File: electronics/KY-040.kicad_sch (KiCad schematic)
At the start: 8 parts, among them SW2 PEC12R-4220F-S0024

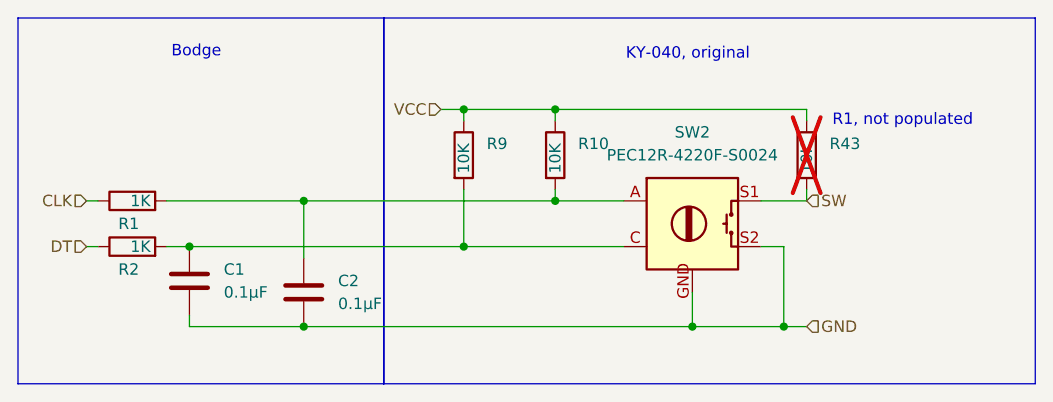
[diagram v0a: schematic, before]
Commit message: docs(electronics): label KY-040 resistors
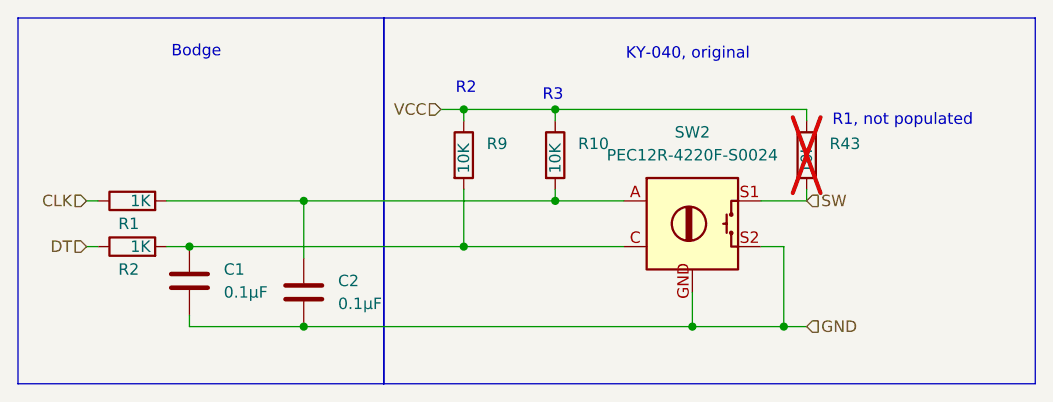
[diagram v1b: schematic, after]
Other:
- note added: "R2"
- note added: "R3"
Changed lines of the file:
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@@
+		)
+	)
+	(text "R2"
+		(exclude_from_sim no)
+		(at 70.104 89.154 0)
+		(effects
+			(font
+				(size 1.27 1.27)
+			)
+		)
+	)
+	(text "R3"
+		(exclude_from_sim no)
+		(at 79.756 89.916 0)
+		(effects
+			(font
+				(size 1.27 1.27)
+			)
 		)
 	)

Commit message: docs(electronics): reformat for readability
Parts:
- R1, R10, R2, R9: symbol Device:R -> Device:R_US
- R43: symbol Device:R -> Device:R_US; now in the parts list
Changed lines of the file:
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@@
 	)
 	(symbol
-		(lib_id "Device:R")
+		(lib_id "Device:R_US")
 		(at 80.01 96.52 0)
 		(unit 1)
@@
 		(dnp no)
 		(property "Reference" "R10"
-			(at 82.55 95.2499 0)
+			(at 75.438 93.98 0)
 			(effects
 				(font
@@
 		)
 		(property "Value" "10K"
-			(at 80.01 98.552 90)
-			(effects
-				(font
-					(size 1.27 1.27)
-				)
-				(justify left)
-			)
-		)
-		(property "Footprint" ""
-			(at 78.232 96.52 90)
+			(at 74.422 97.282 0)
+			(effects
+				(font
+					(size 1.27 1.27)
+				)
+				(justify left)
+			)
+		)
+		(property "Footprint" ""
+			(at 81.026 96.774 90)
 			(effects
 				(font
@@
 			)
 		)
-		(property "Description" "Resistor"
+		(property "Description" "Resistor, US symbol"
 			(at 80.01 96.52 0)
 			(effects
@@
 	)
 	(symbol
-		(lib_id "Device:R")
+		(lib_id "Device:R_US")
 		(at 69.85 96.52 0)
 		(unit 1)
@@
 		(dnp no)
 		(property "Reference" "R9"
-			(at 72.39 95.2499 0)
+			(at 65.532 96.266 0)
 			(effects
 				(font
@@
 		)
 		(property "Value" "10K"
-			(at 69.85 98.552 90)
-			(effects
-				(font
-					(size 1.27 1.27)
-				)
-				(justify left)
-			)
-		)
-		(property "Footprint" ""
-			(at 68.072 96.52 90)
+			(at 64.516 98.298 0)
+			(effects
+				(font
+					(size 1.27 1.27)
+				)
+				(justify left)
+			)
+		)
+		(property "Footprint" ""
+			(at 70.866 96.774 90)
 			(effects
 				(font
@@
 			)
 		)
-		(property "Description" "Resistor"
+		(property "Description" "Resistor, US symbol"
 			(at 69.85 96.52 0)
 			(effects
@@
 	)
 	(symbol
-		(lib_id "Device:R")
+		(lib_id "Device:R_US")
 		(at 33.02 106.68 90)
 		(unit 1)
@@
 		(dnp no)
 		(property "Reference" "R2"
-			(at 33.782 109.22 90)
+			(at 36.068 104.394 90)
 			(effects
 				(font
@@
 		)
 		(property "Value" "1K"
-			(at 35.052 106.68 90)
-			(effects
-				(font
-					(size 1.27 1.27)
-				)
-				(justify left)
-			)
-		)
-		(property "Footprint" ""
-			(at 33.02 108.458 90)
+			(at 31.75 104.648 90)
+			(effects
+				(font
+					(size 1.27 1.27)
+				)
+				(justify left)
+			)
+		)
+		(property "Footprint" ""
+			(at 33.274 105.664 90)
 			(effects
 				(font
@@
 			)
 		)
-		(property "Description" "Resistor"
+		(property "Description" "Resistor, US symbol"
 			(at 33.02 106.68 0)
 			(effects
@@
 	)
 	(symbol
-		(lib_id "Device:R")
+		(lib_id "Device:R_US")
 		(at 107.95 96.52 0)
 		(unit 1)
-		(exclude_from_sim yes)
-		(in_bom no)
+		(exclude_from_sim no)
+		(in_bom yes)
 		(on_board yes)
 		(dnp yes)
 		(property "Reference" "R43"
-			(at 110.49 95.2499 0)
+			(at 109.728 95.25 0)
 			(effects
 				(font
@@
 		)
 		(property "Value" "10K"
-			(at 107.95 98.552 90)
-			(effects
-				(font
-					(size 1.27 1.27)
-				)
-				(justify left)
-			)
-		)
-		(property "Footprint" ""
-			(at 106.172 96.52 90)
+			(at 109.474 97.536 0)
+			(effects
+				(font
+					(size 1.27 1.27)
+				)
+				(justify left)
+			)
+		)
+		(property "Footprint" ""
+			(at 108.966 96.774 90)
 			(effects
 				(font
@@
 			)
 		)
-		(property "Description" "Resistor"
+		(property "Description" "Resistor, US symbol"
 			(at 107.95 96.52 0)
 			(effects
@@
 	)
 	(symbol
-		(lib_id "Device:R")
+		(lib_id "Device:R_US")
 		(at 33.02 101.6 90)
 		(unit 1)
@@
 		(dnp no)
 		(property "Reference" "R1"
-			(at 33.782 104.14 90)
+			(at 36.068 99.568 90)
 			(effects
 				(font
@@
 		)
 		(property "Value" "1K"
-			(at 35.052 101.6 90)
-			(effects
-				(font
-					(size 1.27 1.27)
-				)
-				(justify left)
-			)
-		)
-		(property "Footprint" ""
-			(at 33.02 103.378 90)
+			(at 32.258 99.568 90)
+			(effects
+				(font
+					(size 1.27 1.27)
+				)
+				(justify left)
+			)
+		)
+		(property "Footprint" ""
+			(at 33.274 100.584 90)
 			(effects
 				(font
@@
 			)
 		)
-		(property "Description" "Resistor"
+		(property "Description" "Resistor, US symbol"
 			(at 33.02 101.6 0)
 			(effects
